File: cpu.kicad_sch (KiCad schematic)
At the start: 24 parts, among them J4 Conn_01x40_MountingPin, U1 USBLC6-2SC6, U2 ST1S10PHR, U5 W25Q128JVE, Y2 Crystal_GND24

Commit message: Перевёл на иерархические схемы
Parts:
- removed J4: Conn_01x40_MountingPin, Connector_FFC-FPC:Amphenol_F32R-1A7x1-11040_1x40-1MP_P0.5mm_Horizontal, symbol Connector_Generic_MountingPin:Conn_01x40_MountingPin
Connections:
- net LCD.PWM: now reaches DD4.52 (PD22)
- net LCD.VSYNC: now reaches DD4.53 (PD21)
- net LCD.HSYNC: now reaches DD4.54 (PD20)
- net LCD.B2: now reaches DD4.55 (PD0)
- net LCD.B4: now reaches DD4.57 (PD2)
- net LCD.B5: now reaches DD4.58 (PD3)
- net LCD.B6: now reaches DD4.59 (PD4)
- net LCD.B7: now reaches DD4.60 (PD5)
- net LCD.G2: now reaches DD4.61 (PD6)
- net LCD.G3: now reaches DD4.62 (PD7)
- net LCD.G4: now reaches DD4.63 (PD8)
- net LCD.G5: now reaches DD4.64 (PD9)
- net LCD.G6: now reaches DD4.67 (PD10)
- net LCD.G7: now reaches DD4.68 (PD11)
- net LCD.R3: now reaches DD4.69 (PD13)
- net LCD.R4: now reaches DD4.71 (PD14)
- net LCD.R5: now reaches DD4.72 (PD15)
- net LCD.R6: now reaches DD4.73 (PD16)
- net LCD.R7: now reaches DD4.74 (PD17)
- net LCD.CLK: now reaches DD4.75 (PD18)
- net LCD.DE: now reaches DD4.76 (PD19)

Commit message: Добавил клавиатуру
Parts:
- C17: footprint (none) -> Capacitor_SMD:C_1206_3216Metric_Pad1.33x1.80mm_HandSolder
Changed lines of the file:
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@@
 			)
 		)
-		(property "Footprint" ""
+		(property "Footprint" "Capacitor_SMD:C_1206_3216Metric_Pad1.33x1.80mm_HandSolder"
 			(at 115.8748 191.77 0)
 			(hide yes)

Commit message: кнопки
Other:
- moved on the sheet: C23, C24, R9, Y2
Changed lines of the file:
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@@
 	)
 	(junction
+		(at 204.47 222.25)
+		(diameter 0)
+		(color 0 0 0 0)
+	)
+	(junction
 		(at 99.06 234.95)
 		(diameter 0)
@@
 	)
 	(junction
-		(at 233.68 218.44)
+		(at 223.52 229.87)
 		(diameter 0)
 		(color 0 0 0 0)
@@
 	)
 	(junction
+		(at 204.47 229.87)
+		(diameter 0)
+		(color 0 0 0 0)
+	)
+	(junction
 		(at 127 102.87)
 		(diameter 0)
@@
 	)
 	(junction
-		(at 214.63 210.82)
-		(diameter 0)
-		(color 0 0 0 0)
-	)
-	(junction
 		(at 130.81 191.77)
 		(diameter 0)
@@
 	)
 	(junction
-		(at 214.63 218.44)
-		(diameter 0)
-		(color 0 0 0 0)
-	)
-	(junction
 		(at 139.7 234.95)
 		(diameter 0)
@@
 	)
 	(junction
-		(at 247.65 210.82)
+		(at 237.49 222.25)
 		(diameter 0)
 		(color 0 0 0 0)
@@
 	(wire
 		(pts
-			(xy 229.87 210.82) (xy 214.63 210.82)
+			(xy 219.71 222.25) (xy 204.47 222.25)
 		)
 		(stroke
@@
 	(wire
 		(pts
-			(xy 200.66 218.44) (xy 214.63 218.44)
+			(xy 191.77 229.87) (xy 204.47 229.87)
 		)
 		(stroke
@@
 	(wire
 		(pts
-			(xy 247.65 218.44) (xy 233.68 218.44)
+			(xy 237.49 229.87) (xy 223.52 229.87)
 		)
 		(stroke
@@
 	(wire
 		(pts
-			(xy 214.63 210.82) (xy 207.01 210.82)
+			(xy 204.47 222.25) (xy 191.77 222.25)
 		)
 		(stroke
@@
 	(wire
 		(pts
-			(xy 237.49 210.82) (xy 247.65 210.82)
+			(xy 227.33 222.25) (xy 237.49 222.25)
 		)
 		(stroke
@@
 	(wire
 		(pts
-			(xy 247.65 210.82) (xy 257.81 210.82)
+			(xy 237.49 222.25) (xy 247.65 222.25)
 		)
 		(stroke
@@
 	(wire
 		(pts
-			(xy 233.68 218.44) (xy 233.68 215.9)
+			(xy 223.52 229.87) (xy 223.52 227.33)
 		)
 		(stroke
@@
 	(wire
 		(pts
-			(xy 219.71 194.31) (xy 212.09 194.31)
+			(xy 219.71 200.66) (xy 212.09 200.66)
 		)
 		(stroke
@@
 	(wire
 		(pts
-			(xy 214.63 218.44) (xy 233.68 218.44)
+			(xy 204.47 229.87) (xy 223.52 229.87)
 		)
 		(stroke
@@
 	(wire
 		(pts
-			(xy 281.94 170.18) (xy 281.94 194.31)
+			(xy 281.94 170.18) (xy 281.94 200.66)
 		)
 		(stroke
@@
 	(wire
 		(pts
-			(xy 227.33 194.31) (xy 281.94 194.31)
+			(xy 227.33 200.66) (xy 281.94 200.66)
 		)
 		(stroke
@@
 	)
 	(label "XTAL_OUT"
-		(at 257.81 210.82 0)
+		(at 247.65 222.25 0)
 		(effects
 			(font
@@
 	)
 	(label "XTAL_IN"
-		(at 207.01 210.82 0)
+		(at 191.77 222.25 0)
 		(effects
 			(font
@@
 	)
 	(label "RFGND"
-		(at 212.09 194.31 180)
+		(at 212.09 200.66 180)
 		(effects
 			(font
@@
 	)
 	(label "RFDND"
-		(at 200.66 218.44 0)
+		(at 191.77 229.87 0)
 		(effects
 			(font
@@
 	(symbol
 		(lib_id "Device:Crystal_GND24")
-		(at 233.68 210.82 0)
+		(at 223.52 222.25 0)
 		(unit 1)
 		(body_style 1)
@@
 		(fields_autoplaced yes)
 		(property "Reference" "Y2"
-			(at 233.68 201.93 0)
+			(at 223.52 213.36 0)
 			(show_name no)
 			(do_not_autoplace no)
@@
 		)
 		(property "Value" "Crystal_GND24"
-			(at 233.68 204.47 0)
+			(at 223.52 215.9 0)
 			(show_name no)
 			(do_not_autoplace no)
@@
 		)
 		(property "Footprint" "Crystal:Crystal_SMD_7050-4Pin_7.0x5.0mm"
-			(at 233.68 210.82 0)
+			(at 223.52 222.25 0)
 			(hide yes)
 			(show_name no)
@@
 		)
 		(property "Datasheet" ""
-			(at 233.68 210.82 0)
+			(at 223.52 222.25 0)
 			(hide yes)
 			(show_name no)
@@
 		)
 		(property "Description" "Four pin crystal, GND on pins 2 and 4"
-			(at 233.68 210.82 0)
+			(at 223.52 222.25 0)
 			(hide yes)
 			(show_name no)
@@
 		)
 		(property private "KLC_S3.3" "The rectangle is not a symbol body but a graphical element"
-			(at 233.68 223.52 0)
+			(at 223.52 234.95 0)
 			(hide yes)
 			(show_name yes)
@@
 		)
 		(property private "KLC_S4.1" "Some pins are on 50mil grid to make the symbol small"
-			(at 233.68 226.06 0)
+			(at 223.52 237.49 0)
 			(hide yes)
 			(show_name yes)
@@
 	(symbol
 		(lib_id "Device:C")
-		(at 214.63 214.63 0)
+		(at 204.47 226.06 0)
 		(unit 1)
 		(body_style 1)
@@
 		(fields_autoplaced yes)
 		(property "Reference" "C23"
-			(at 218.44 213.3599 0)
+			(at 208.28 224.7899 0)
 			(show_name no)
 			(do_not_autoplace no)
@@
 		)
 		(property "Value" "22 pF"
-			(at 218.44 215.8999 0)
+			(at 208.28 227.3299 0)
 			(show_name no)
 			(do_not_autoplace no)
@@
 		)
 		(property "Footprint" "Capacitor_SMD:C_0805_2012Metric_Pad1.18x1.45mm_HandSolder"
-			(at 215.5952 218.44 0)
+			(at 205.4352 229.87 0)
 			(hide yes)
 			(show_name no)
@@
 		)
 		(property "Datasheet" ""
-			(at 214.63 214.63 0)
+			(at 204.47 226.06 0)
 			(hide yes)
 			(show_name no)
@@
 		)
 		(property "Description" "Unpolarized capacitor"
-			(at 214.63 214.63 0)
+			(at 204.47 226.06 0)
 			(hide yes)
 			(show_name no)
@@
 	(symbol
 		(lib_id "Device:R")
-		(at 223.52 194.31 90)
+		(at 223.52 200.66 90)
 		(unit 1)
 		(body_style 1)
@@
 		(fields_autoplaced yes)
 		(property "Reference" "R9"
-			(at 223.52 187.96 90)
+			(at 223.52 194.31 90)
 			(show_name no)
 			(do_not_autoplace no)
@@
 		)
 		(property "Value" "240 R F"
-			(at 223.52 190.5 90)
+			(at 223.52 196.85 90)
 			(show_name no)
 			(do_not_autoplace no)
@@
 		)
 		(property "Footprint" "Resistor_SMD:R_0805_2012Metric_Pad1.20x1.40mm_HandSolder"
-			(at 223.52 196.088 90)
+			(at 223.52 202.438 90)
 			(hide yes)
 			(show_name no)
@@
 		)
 		(property "Datasheet" ""
-			(at 223.52 194.31 0)
+			(at 223.52 200.66 0)
 			(hide yes)
 			(show_name no)
@@
 		)
 		(property "Description" "Resistor"
-			(at 223.52 194.31 0)
+			(at 223.52 200.66 0)
 			(hide yes)
 			(show_name no)
@@
 	(symbol
 		(lib_id "Device:C")
-		(at 247.65 214.63 0)
+		(at 237.49 226.06 0)
 		(unit 1)
 		(body_style 1)
@@
 		(fields_autoplaced yes)
 		(property "Reference" "C24"
-			(at 251.46 213.3599 0)
+			(at 241.3 224.7899 0)
 			(show_name no)
 			(do_not_autoplace no)
@@
 		)
 		(property "Value" "22 pF"
-			(at 251.46 215.8999 0)
+			(at 241.3 227.3299 0)
 			(show_name no)
 			(do_not_autoplace no)
@@
 		)
 		(property "Footprint" "Capacitor_SMD:C_0805_2012Metric_Pad1.18x1.45mm_HandSolder"
-			(at 248.6152 218.44 0)
+			(at 238.4552 229.87 0)
 			(hide yes)
 			(show_name no)
@@
 		)
 		(property "Datasheet" ""
-			(at 247.65 214.63 0)
+			(at 237.49 226.06 0)
 			(hide yes)
 			(show_name no)
@@
 		)
 		(property "Description" "Unpolarized capacitor"
-			(at 247.65 214.63 0)
+			(at 237.49 226.06 0)
 			(hide yes)
 			(show_name no)

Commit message: save state
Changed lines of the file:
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@@
-		)
-	)
-	(global_label "LCD{R[2..7] G[1..7] B[2..7] CLK DE VSYNC HSYNC PWM}"
-		(shape input)
-		(at 349.25 222.25 0)
-		(fields_autoplaced yes)
-		(effects
-			(font
-				(size 1.27 1.27)
-			)
-			(justify left)
-		)
-		(property "Intersheetrefs" "${INTERSHEET_REFS}"
-			(at 406.4221 222.25 0)
-			(hide yes)
-			(show_name no)
-			(do_not_autoplace no)
-			(effects
-				(font
-					(size 1.27 1.27)
-				)
-				(justify left)
-			)
 		)
 	)
@@
 		)
 	)
+	(hierarchical_label "LCD{R[2..7] G[1..7] B[2..7] CLK DE VSYNC HSYNC PWM}"
+		(shape bidirectional)
+		(at 349.25 222.25 0)
+		(effects
+			(font
+				(size 1.27 1.27)
+			)
+			(justify left)
+		)
+	)

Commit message: Использование power symbols
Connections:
- net RFDND: no longer C23.2, C24.2, Y2.2 (G), Y2.4 (G)
- net RFGND: now also C23.2, C24.2, Y2.2 (G), Y2.4 (G)

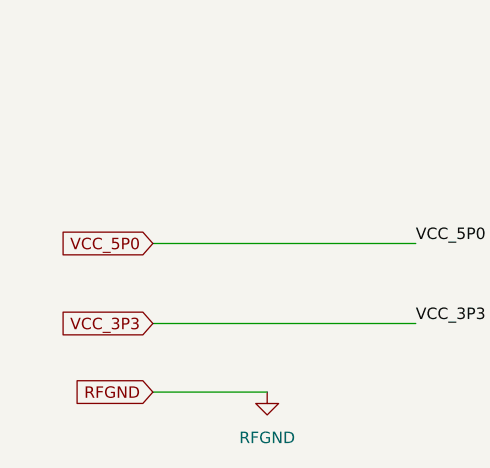
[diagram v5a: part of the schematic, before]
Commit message: add lcd backlight chip
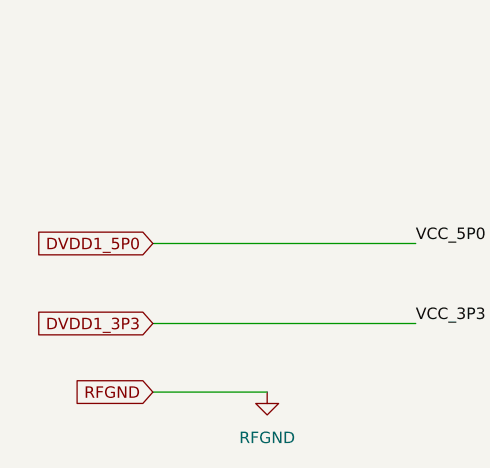
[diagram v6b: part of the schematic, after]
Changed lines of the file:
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@@
+		)
+	)
+	(global_label "DVDD1_3P3"
+		(shape input)
+		(at 33.02 264.16 180)
+		(fields_autoplaced yes)
+		(effects
+			(font
+				(size 1.27 1.27)
+			)
+			(justify right)
+		)
+		(property "Intersheetrefs" "${INTERSHEET_REFS}"
+			(at 19.2701 264.16 0)
+			(hide yes)
+			(show_name no)
+			(do_not_autoplace no)
+			(effects
+				(font
+					(size 1.27 1.27)
+				)
+				(justify right)
+			)
+		)
+	)
+	(global_label "DVDD1_5P0"
+		(shape input)
+		(at 33.02 255.27 180)
+		(fields_autoplaced yes)
+		(effects
+			(font
+				(size 1.27 1.27)
+			)
+			(justify right)
+		)
+		(property "Intersheetrefs" "${INTERSHEET_REFS}"
+			(at 19.2701 255.27 0)
+			(hide yes)
+			(show_name no)
+			(do_not_autoplace no)
+			(effects
+				(font
+					(size 1.27 1.27)
+				)
+				(justify right)
+			)
 		)
 	)
@@
 			(hide yes)
 			(show_name no)
-			(do_not_autoplace no)
-			(effects
-				(font
-					(size 1.27 1.27)
-				)
-				(justify right)
-			)
-		)
-	)
-	(global_label "VCC_3P3"
-		(shape input)
-		(at 33.02 264.16 180)
-		(fields_autoplaced yes)
-		(effects
-			(font
-				(size 1.27 1.27)
-			)
-			(justify right)
-		)
-		(property "Intersheetrefs" "${INTERSHEET_REFS}"
-			(at 21.7496 264.16 0)
-			(hide yes)
-			(show_name no)
-			(do_not_autoplace no)
-			(effects
-				(font
-					(size 1.27 1.27)
-				)
-				(justify right)
-			)
-		)
-	)
-	(global_label "VCC_5P0"
-		(shape input)
-		(at 33.02 255.27 180)
-		(fields_autoplaced yes)
-		(effects
-			(font
-				(size 1.27 1.27)
-			)
-			(justify right)
-		)
-		(property "Intersheetrefs" "${INTERSHEET_REFS}"
-			(at 21.7496 255.27 0)
-			(hide yes)
-			(show_name no)
